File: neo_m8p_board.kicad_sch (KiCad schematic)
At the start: 14 parts, among them J1 SMA, J3 Conn_01x05, J4 Conn_01x06, U1 NEO-M8P

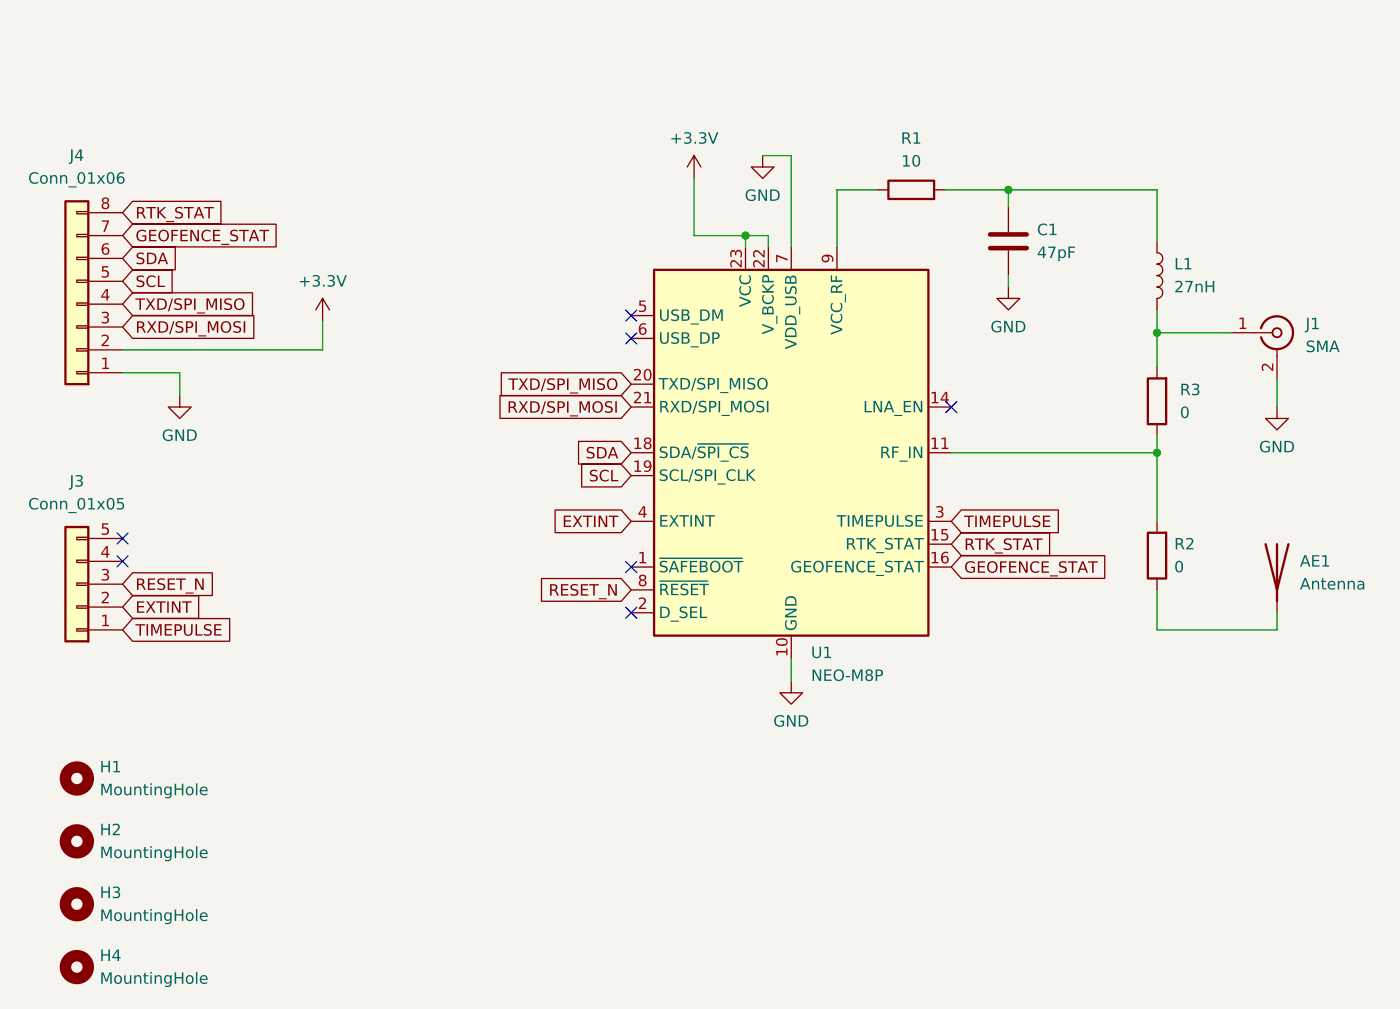
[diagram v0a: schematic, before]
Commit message: v2: sma antenna only
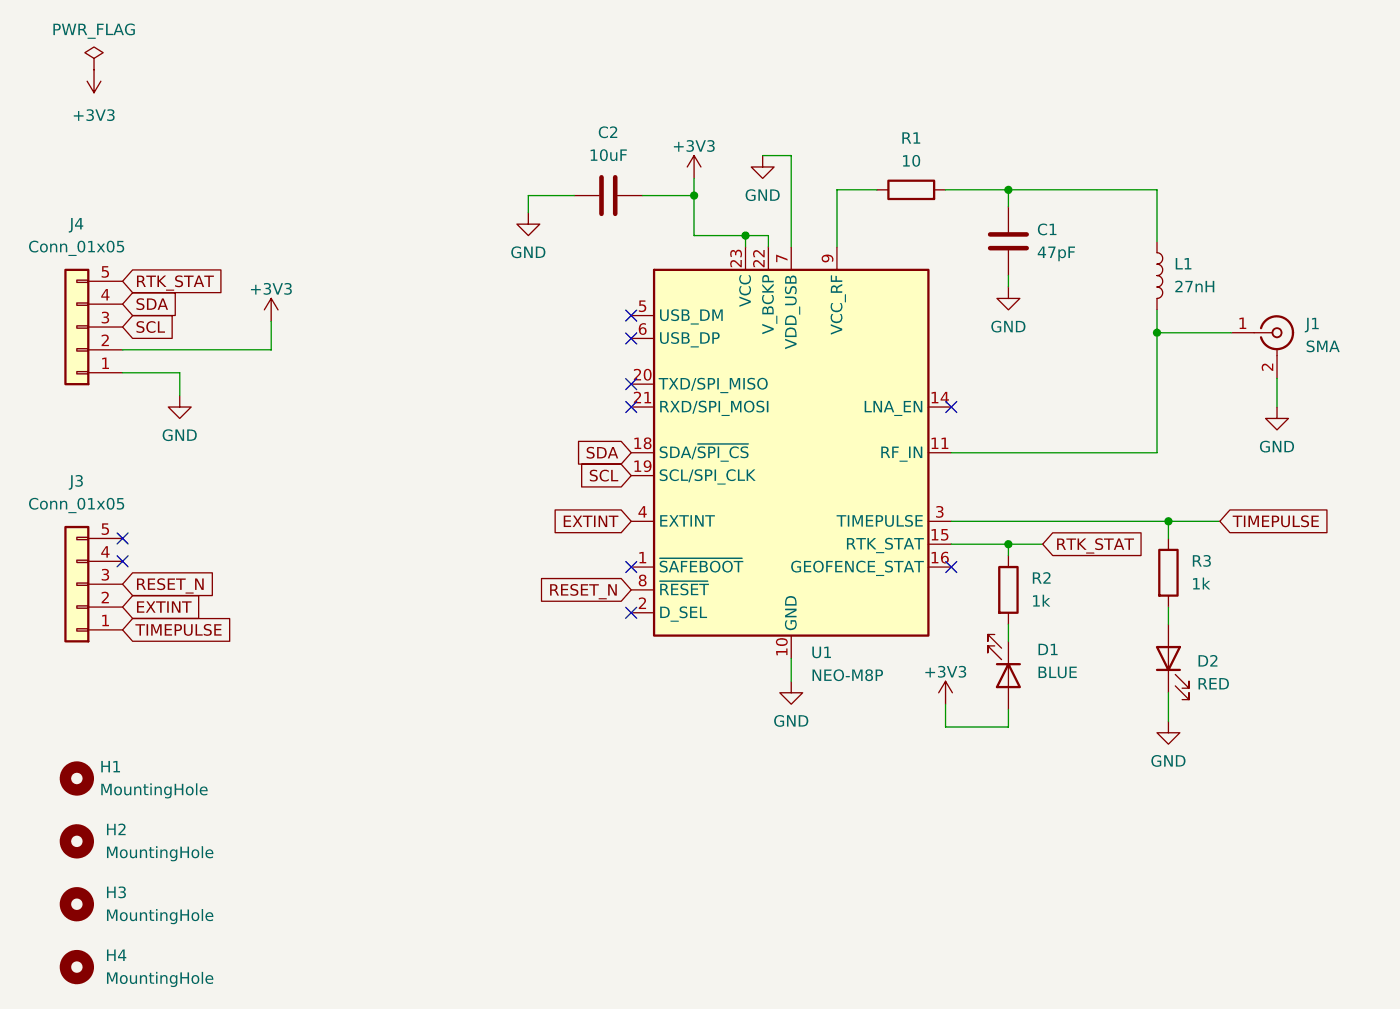
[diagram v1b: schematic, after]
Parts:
- removed AE1: Antenna, NEO-M8P-Library:GPS_Patch_Antenna_Amphenol, symbol Device:Antenna
- removed J4: Conn_01x06, Connector_PinHeader_2.54mm:PinHeader_1x08_P2.54mm_Vertical, symbol Connector_Generic:Conn_01x08
- added C2: 10uF, Capacitor_SMD:C_0805_2012Metric_Pad1.18x1.45mm_HandSolder, symbol Device:C
- added D1: BLUE, LED_SMD:LED_0805_2012Metric_Pad1.15x1.40mm_HandSolder, symbol Device:LED
- added D2: RED, LED_SMD:LED_0805_2012Metric_Pad1.15x1.40mm_HandSolder, symbol Device:LED
- added J4: Conn_01x05, Connector_PinHeader_2.54mm:PinHeader_1x05_P2.54mm_Vertical, symbol Connector_Generic:Conn_01x05
- H1, H2, H3, H4: footprint MountingHole:MountingHole_2.2mm_M2 -> MountingHole:MountingHole_3.2mm_M3
- R2, R3: value 0 -> 1k; LCSC (none) -> C17513
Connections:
- net GND: now also C2.1, D2.1 (K), J4.1 (Pin_1)
- net RTK_STAT: now also R2.1, J4.5 (Pin_5)
- net SCL: now also J4.3 (Pin_3)
- net SDA: now also J4.4 (Pin_4)
- net TIMEPULSE: now also R3.1
- net at J1.1 (In), L1.2: now also U1.11 (RF_IN); no longer R3.2
- net +3.3V renamed +3V3
- net +3V3: now also C2.2, D1.2 (A), J4.2 (Pin_2)
- net GEOFENCE_STAT: no longer names the net of U1.16 (GEOFENCE_STAT)
- net RXD/SPI_MOSI: no longer names the net of U1.21 (RXD/SPI_MOSI)
- net TXD/SPI_MISO: no longer names the net of U1.20 (TXD/SPI_MISO)
- new net: D2.2 (A), R3.2
- new net: D1.1 (K), R2.2
- no-connect marks 7 -> 10
